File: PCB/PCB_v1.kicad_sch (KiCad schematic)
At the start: 1 part, among them U1 Teensy4.0

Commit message: Finish KiCad Schematic
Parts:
- added J1: Accelerometer, symbol Connector:Conn_01x04_Socket
- added J2: Flysky FS2A Receiver, symbol Connector:Conn_01x12_Pin
- added J3: DC-DC, symbol Connector:Conn_01x04_Pin
- added J4: Battery Left, symbol Connector:Conn_01x02_Pin
- added J5: Battery Right, symbol Connector:Conn_01x02_Pin
- added J6: ESC Left, symbol Connector:Conn_01x05_Pin
- added J7: ESC Right, symbol Connector:Conn_01x05_Pin
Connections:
- net SDA_18: now reaches U1.25 (18_A4_SDA0)
- net SDA_18: now also J1.3 (Pin_3)
- net SCL_19: now reaches U1.26 (19_A5_SCL0)
- net SCL_19: now also J1.4 (Pin_4)
- net CH4_20: now reaches U1.27 (20_A6_TX5_LRCLK1)
- net CH4_20: now also J2.4 (Pin_4)
- net CH3_21: now reaches U1.28 (21_A7_RX5_BCLK1)
- net CH3_21: now also J2.3 (Pin_3)
- net CH2_22: now reaches U1.29 (22_A8_CTX1)
- net CH2_22: now also J2.2 (Pin_2)
- net CH1_23: now reaches U1.30 (23_A9_CRX1_MCLK1)
- net CH1_23: now also J2.1 (Pin_1)
- net 3.3V: now reaches U1.31 (3V3)
- net 3.3V: now also J1.2 (Pin_2), J2.5 (Pin_5), J2.6 (Pin_6), J2.7 (Pin_7), J2.8 (Pin_8)
- net GND: now reaches U1.32 (GND)
- net GND: now also J1.1 (Pin_1), J2.10 (Pin_10), J2.11 (Pin_11), J2.12 (Pin_12), J2.9 (Pin_9), J3.2 (Pin_2), J3.4 (Pin_4), J4.2 (Pin_2), J5.2 (Pin_2), J6.1 (Pin_1), J6.2 (Pin_2), J7.1 (Pin_1), J7.2 (Pin_2)
- net 5V: now reaches U1.33 (VIN)
- net 5V: now also J3.3 (Pin_3)
- net S_ESC_Left_2: now reaches U1.4 (2_OUT2)
- net S_ESC_Left_2: now also J6.3 (Pin_3)
- net S_ESC_Right_3: now reaches U1.5 (3_LRCLK2)
- net S_ESC_Right_3: now also J7.3 (Pin_3)
- new net 12V: J3.1 (Pin_1), J4.1 (Pin_1), J5.1 (Pin_1), J6.5 (Pin_5), J7.5 (Pin_5)
- no-connect marks 0 -> 2
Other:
- moved on the sheet: U1

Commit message: Import Teensy Footprints
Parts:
- U1: footprint (none) -> Teensy:Teensy40
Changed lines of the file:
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@@
 			)
 		)
-		(property "Footprint" ""
+		(property "Footprint" "Teensy:Teensy40"
 			(at 160.02 105.41 0)
 			(effects

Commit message: Create Footprint for DC_DC
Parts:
- J3: footprint (none) -> Suffed Crust:DC_DC
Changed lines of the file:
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@@
 			)
 		)
-		(property "Footprint" ""
+		(property "Footprint" "Suffed Crust:DC_DC"
 			(at 91.44 110.49 0)
 			(effects

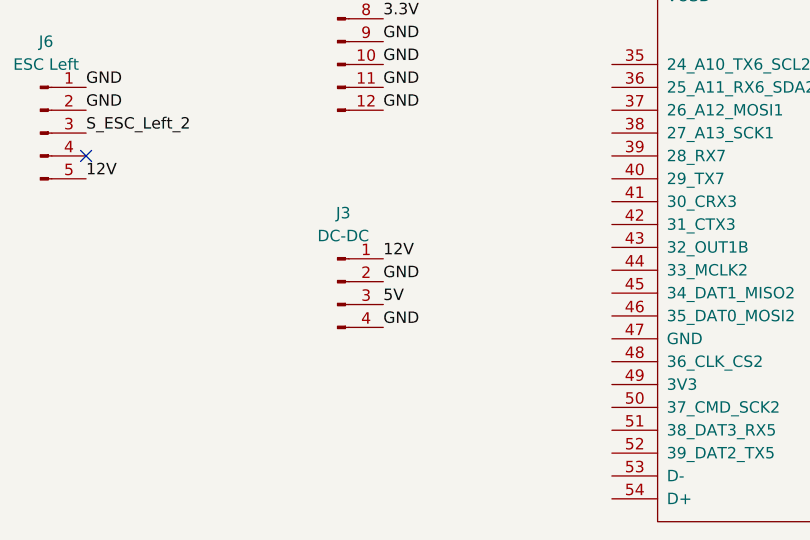
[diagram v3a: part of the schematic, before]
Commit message: Update DC_DC Footprint
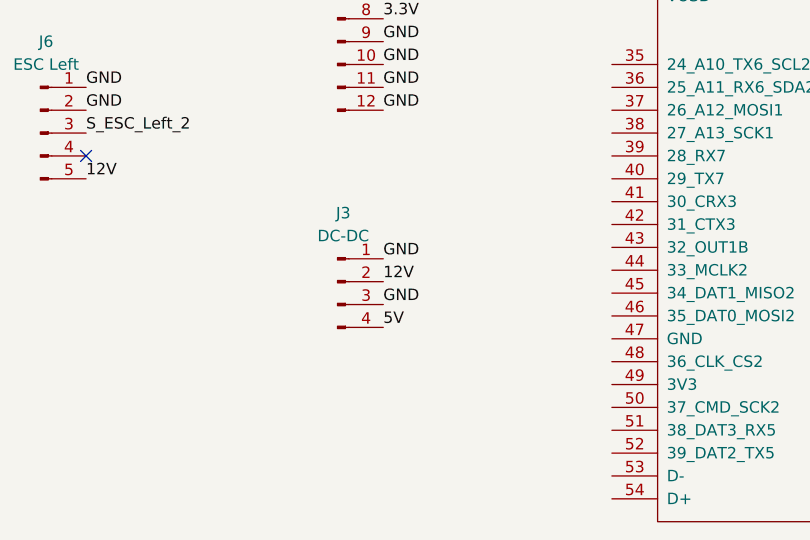
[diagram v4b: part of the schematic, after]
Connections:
- net 12V: now also J3.2 (Pin_2); no longer J3.1 (Pin_1)
- net 5V: now also J3.4 (Pin_4); no longer J3.3 (Pin_3)
- net GND: now also J3.1 (Pin_1), J3.3 (Pin_3); no longer J3.2 (Pin_2), J3.4 (Pin_4)
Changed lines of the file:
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@@
+		)
+	)
+	(label "GND"
+		(at 96.52 107.95 0)
+		(effects
+			(font
+				(size 1.27 1.27)
+			)
+			(justify left bottom)
 		)
 	)
@@
 		)
 	)
+	(label "12V"
+		(at 96.52 110.49 0)
+		(effects
+			(font
+				(size 1.27 1.27)
+			)
+			(justify left bottom)
+		)
+	)
 	(label "SCL_19"
 		(at 196.85 72.39 180)
@@
 		)
 	)
-	(label "GND"
-		(at 96.52 110.49 0)
-		(effects
-			(font
-				(size 1.27 1.27)
-			)
-			(justify left bottom)
-		)
-	)
 	(label "CH3_21"
 		(at 96.52 68.58 0)
@@
 		)
 	)
-	(label "12V"
-		(at 96.52 107.95 0)
+	(label "GND"
+		(at 96.52 113.03 0)
 		(effects
 			(font
@@
 		)
 	)
+	(label "3.3V"
+		(at 121.92 71.12 180)
+		(effects
+			(font
+				(size 1.27 1.27)
+			)
+			(justify right bottom)
+		)
+	)
 	(label "5V"
-		(at 96.52 113.03 0)
-		(effects
-			(font
-				(size 1.27 1.27)
-			)
-			(justify left bottom)
-		)
-	)
-	(label "3.3V"
-		(at 121.92 71.12 180)
-		(effects
-			(font
-				(size 1.27 1.27)
-			)
-			(justify right bottom)
+		(at 96.52 115.57 0)
+		(effects
+			(font
+				(size 1.27 1.27)
+			)
+			(justify left bottom)
 		)
 	)
@@
 		(effects
 			(font
-				(size 1.27 1.27)
-			)
-			(justify left bottom)
-		)
-	)
-	(label "GND"
-		(at 96.52 115.57 0)
-		(effects
-			(font

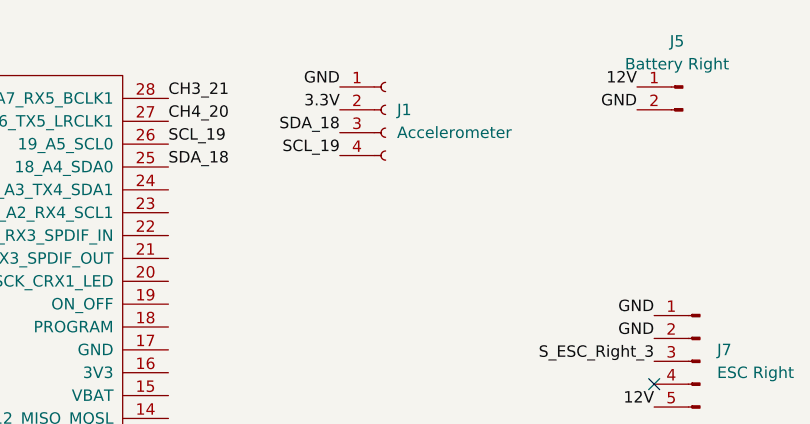
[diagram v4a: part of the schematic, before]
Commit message: Add and Link the Footprint of Flysky FS2A Receiver
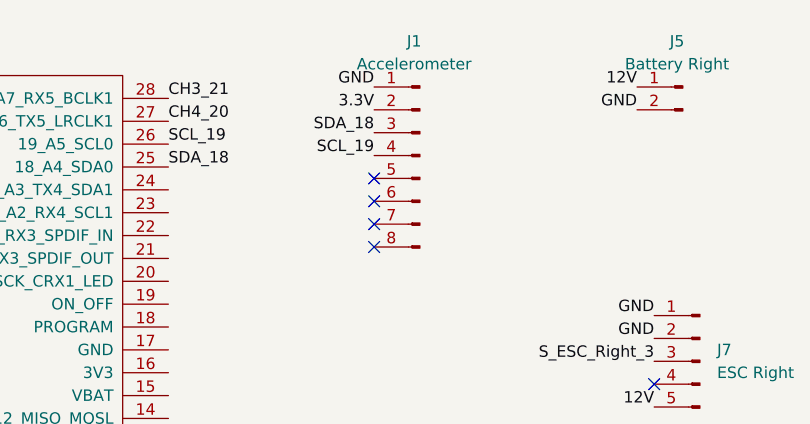
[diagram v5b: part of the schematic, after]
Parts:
- removed J1: Accelerometer, symbol Connector:Conn_01x04_Socket
- added J1: Accelerometer, symbol Connector:Conn_01x08_Pin
- J2: footprint (none) -> Stuffed Crust:Flysky_FS2A_Receiver
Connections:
- net 3.3V: now also J1.2 (Pin_2)
- net GND: now also J1.1 (Pin_1)
- net SCL_19: now also J1.4 (Pin_4)
- net SDA_18: now also J1.3 (Pin_3)
- no-connect marks 2 -> 6
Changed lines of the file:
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@@
+	)
+	(no_connect
+		(at 200.66 74.93)
 	)
 	(no_connect
@@
 	)
 	(no_connect
+		(at 200.66 77.47)
+	)
+	(no_connect
+		(at 200.66 82.55)
+	)
+	(no_connect
 		(at 231.775 97.79)
 	)
+	(no_connect
+		(at 200.66 80.01)
+	)
 	(label "3.3V"
-		(at 196.85 67.31 180)
+		(at 200.66 67.31 180)
 		(effects
 			(font
@@
 	)
 	(label "SDA_18"
-		(at 196.85 69.85 180)
+		(at 200.66 69.85 180)
 		(effects
 			(font
@@
 	)
 	(label "GND"
-		(at 196.85 64.77 180)
+		(at 200.66 64.77 180)
 		(effects
 			(font
@@
 	)
 	(label "SCL_19"
-		(at 196.85 72.39 180)
+		(at 200.66 72.39 180)
 		(effects
 			(font
@@
 			)
 		)
-		(property "Footprint" ""
+		(property "Footprint" "Stuffed Crust:Flysky_FS2A_Receiver"
 			(at 91.44 76.2 0)
 			(effects
@@
 	)
 	(symbol
-		(lib_id "Connector:Conn_01x04_Socket")
-		(at 201.93 67.31 0)
+		(lib_id "Connector:Conn_01x08_Pin")
+		(at 205.74 72.39 0)
+		(mirror y)
 		(unit 1)
 		(exclude_from_sim no)
@@
 		(on_board yes)
 		(dnp no)
-		(fields_autoplaced yes)
 		(property "Reference" "J1"
-			(at 203.2 67.3099 0)
-			(effects
-				(font
-					(size 1.27 1.27)
-				)
-				(justify left)
+			(at 205.105 59.69 0)
+			(effects
+				(font
+					(size 1.27 1.27)
+				)
 			)
 		)
 		(property "Value" "Accelerometer"
-			(at 203.2 69.8499 0)
-			(effects
-				(font
-					(size 1.27 1.27)
-				)
-				(justify left)
+			(at 205.105 62.23 0)
+			(effects
+				(font
+					(size 1.27 1.27)
+				)
 			)
 		)
 		(property "Footprint" ""
-			(at 201.93 67.31 0)
+			(at 205.74 72.39 0)
 			(effects
 				(font
@@
 		)
 		(property "Datasheet" "~"
-			(at 201.93 67.31 0)
-			(effects
-				(font
-					(size 1.27 1.27)
-				)
-				(hide yes)
-			)
-		)
-		(property "Description" "Generic connector, single row, 01x04, script generated"
-			(at 201.93 67.31 0)
-			(effects
-				(font
-					(size 1.27 1.27)
-				)
-				(hide yes)
-			)
+			(at 205.74 72.39 0)
+			(effects
+				(font
+					(size 1.27 1.27)
+				)
+				(hide yes)
+			)
+		)
+		(property "Description" "Generic connector, single row, 01x08, script generated"
+			(at 205.74 72.39 0)
+			(effects
+				(font
+					(size 1.27 1.27)
+				)
+				(hide yes)
+			)
+		)
+		(pin "6"
+		)
+		(pin "7"
+		)
+		(pin "8"
+		)
+		(pin "5"
+		)
+		(pin "4"
+		)
+		(pin "2"
+		)
+		(pin "3"
 		)
 		(pin "1"
 		)
-		(pin "2"
-		)
-		(pin "3"
-		)
-		(pin "4"
-		)
 		(instances

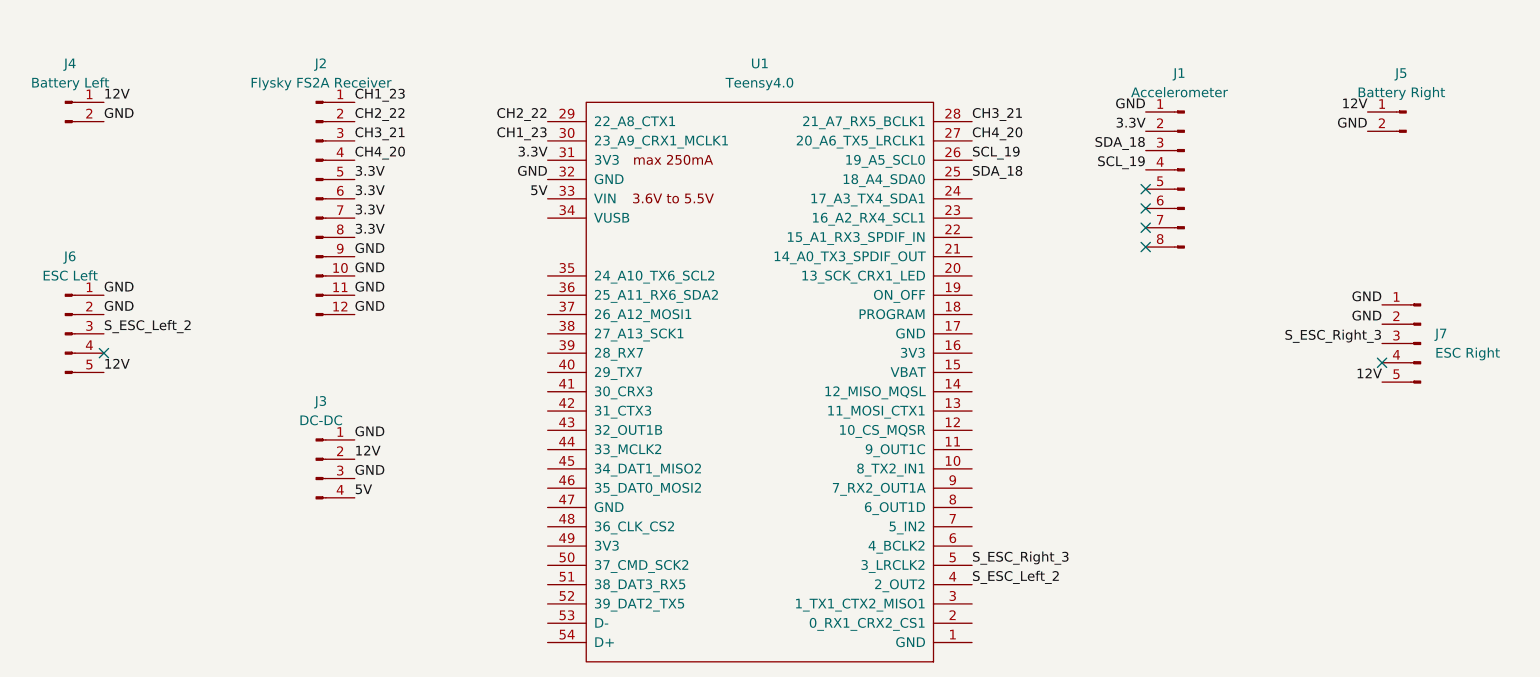
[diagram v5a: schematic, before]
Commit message: Add LED Connector
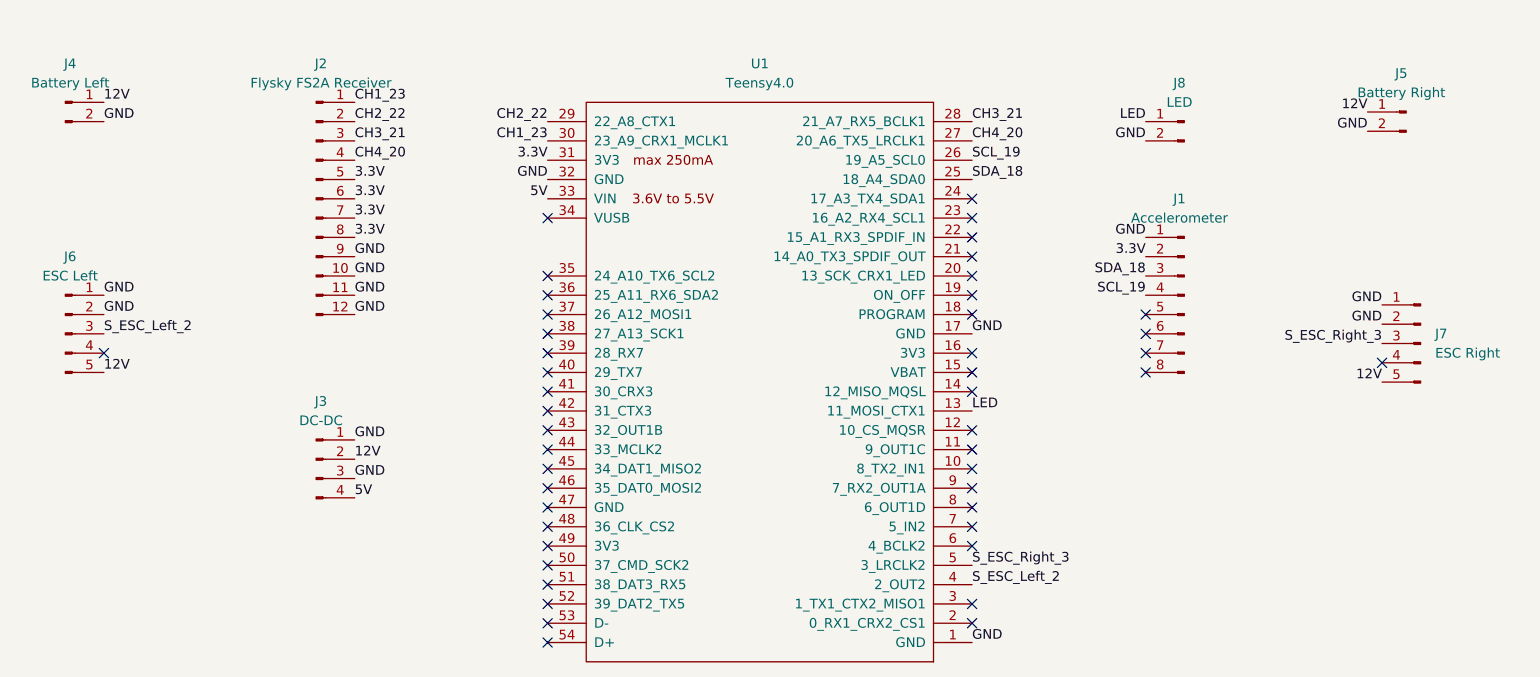
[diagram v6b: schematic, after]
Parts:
- added J8: LED, symbol Connector:Conn_01x02_Pin
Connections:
- net GND: now also U1.1 (GND), U1.17 (GND), J8.2 (Pin_2)
- net LED: now reaches U1.13 (11_MOSI_CTX1)
- net LED: now also J8.1 (Pin_1)
- no-connect marks 6 -> 46
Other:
- moved on the sheet: J1

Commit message: Finish the schematics and footprints of ESC, LED and Battery
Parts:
- J4, J5, J8: footprint (none) -> Stuffed Crust:Battery_or_LED
- J6, J7: footprint (none) -> Stuffed Crust:ESC
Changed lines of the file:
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@@
 			)
 		)
-		(property "Footprint" ""
+		(property "Footprint" "Stuffed Crust:ESC"
 			(at 58.42 93.98 0)
 			(effects
@@
 			)
 		)
-		(property "Footprint" ""
+		(property "Footprint" "Stuffed Crust:ESC"
 			(at 236.855 95.25 0)
 			(effects
@@
 			)
 		)
-		(property "Footprint" ""
+		(property "Footprint" "Stuffed Crust:Battery_or_LED"
 			(at 205.74 66.04 0)
 			(effects
@@
 			)
 		)
-		(property "Footprint" ""
+		(property "Footprint" "Stuffed Crust:Battery_or_LED"
 			(at 58.42 63.5 0)
 			(effects
@@
 			)
 		)
-		(property "Footprint" ""
+		(property "Footprint" "Stuffed Crust:Battery_or_LED"
 			(at 234.95 64.77 0)
 			(effects

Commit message: Accelerometer Footprint
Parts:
- J1: footprint (none) -> Stuffed Crust:Accelerometer
- J3: footprint Suffed Crust:DC_DC -> Stuffed Crust:DC_DC
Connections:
- net 3.3V: now also J1.6 (Pin_6); no longer J1.2 (Pin_2)
- net GND: now also J1.5 (Pin_5); no longer J1.1 (Pin_1)
- net SCL_19: now also J1.8 (Pin_8); no longer J1.4 (Pin_4)
- net SDA_18: now also J1.7 (Pin_7); no longer J1.3 (Pin_3)
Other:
- note added: "These pins are on the bottom of Teensy 4.0"
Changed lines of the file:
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@@
 		(title "Stuffed Crust")
 	)
+	(text "These pins are on the bottom of Teensy 4.0"
+		(exclude_from_sim no)
+		(at 118.11 109.982 90)
+		(effects
+			(font
+				(size 1.27 1.27)
+			)
+			(justify top)
+		)
+	)
 	(no_connect
 		(at 121.92 96.52)
@@
 	)
 	(no_connect
-		(at 200.66 91.44)
-	)
-	(no_connect
 		(at 121.92 114.3)
 	)
@@
 	)
 	(no_connect
+		(at 200.66 86.36)
+	)
+	(no_connect
+		(at 200.66 81.28)
+	)
+	(no_connect
 		(at 177.8 109.22)
 	)
@@
 	)
 	(no_connect
-		(at 200.66 93.98)
-	)
-	(no_connect
 		(at 121.92 124.46)
 	)
@@
 	)
 	(no_connect
-		(at 200.66 99.06)
-	)
-	(no_connect
 		(at 177.8 83.82)
 	)
@@
 	)
 	(no_connect
+		(at 200.66 83.82)
+	)
+	(no_connect
 		(at 231.775 97.79)
 	)
@@
 	)
 	(no_connect
-		(at 200.66 96.52)
-	)
-	(no_connect
 		(at 121.92 129.54)
 	)
 	(no_connect
+		(at 200.66 88.9)
+	)
+	(no_connect
 		(at 177.8 99.06)
 	)
@@
 	(no_connect
 		(at 177.8 114.3)
-	)
-	(label "3.3V"
-		(at 200.66 83.82 180)
-		(effects
-			(font
-				(size 1.27 1.27)
-			)
-			(justify right bottom)
-		)
 	)
 	(label "3.3V"
@@
 		)
 	)
-	(label "SDA_18"
-		(at 200.66 86.36 180)
-		(effects
-			(font
-				(size 1.27 1.27)
-			)
-			(justify right bottom)
-		)
-	)
 	(label "GND"
 		(at 177.8 93.98 0)
@@
 		)
 	)
-	(label "GND"
-		(at 200.66 81.28 180)
+	(label "SCL_19"
+		(at 200.66 99.06 180)
+		(effects
+			(font
+				(size 1.27 1.27)
+			)
+			(justify right bottom)
+		)
+	)
+	(label "GND"
+		(at 200.66 91.44 180)
 		(effects
 			(font
@@
 		)
 	)
+	(label "SDA_18"
+		(at 200.66 96.52 180)
+		(effects
+			(font
+				(size 1.27 1.27)
+			)
+			(justify right bottom)
+		)
+	)
 	(label "SCL_19"
 		(at 177.8 71.12 0)
@@
 		)
 	)
-	(label "SCL_19"
-		(at 200.66 88.9 180)
-		(effects
-			(font
-				(size 1.27 1.27)
-			)
-			(justify right bottom)
-		)
-	)
 	(label "CH3_21"
 		(at 177.8 66.04 0)
@@
 			)
 			(justify left bottom)
+		)
+	)
+	(label "3.3V"
+		(at 200.66 93.98 180)
+		(effects
+			(font
+				(size 1.27 1.27)
+			)
+			(justify right bottom)
 		)
 	)
@@
 			)
 		)
-		(property "Footprint" "Suffed Crust:DC_DC"
+		(property "Footprint" "Stuffed Crust:DC_DC"
 			(at 91.44 110.49 0)
 			(effects
@@
 			)
 		)
-		(property "Footprint" ""
+		(property "Footprint" "Stuffed Crust:Accelerometer"
 			(at 205.74 88.9 0)
 			(effects
